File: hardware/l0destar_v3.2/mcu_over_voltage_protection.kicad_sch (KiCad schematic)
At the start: 15 parts

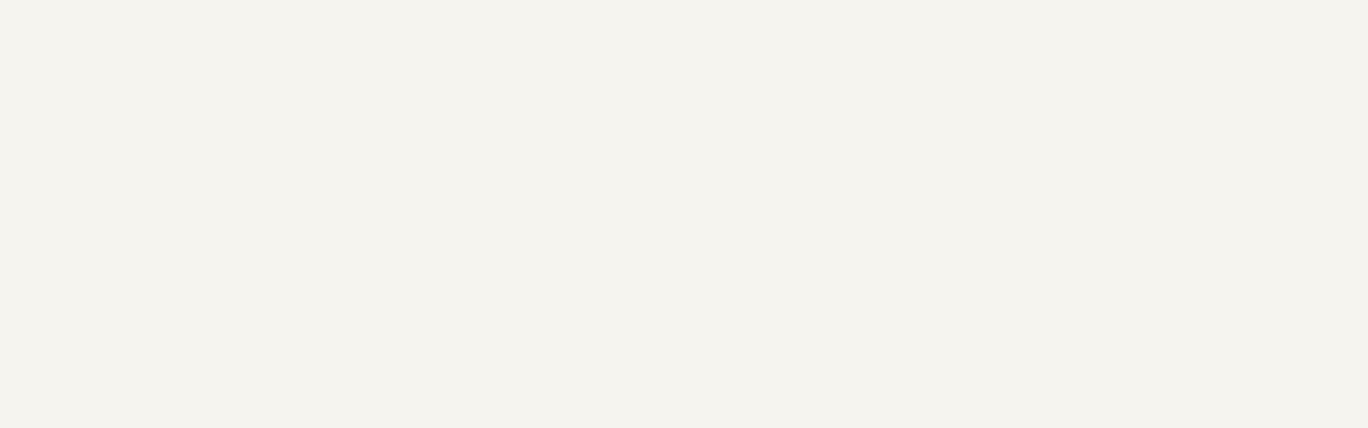
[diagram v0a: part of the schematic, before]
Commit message: update sheet annotations
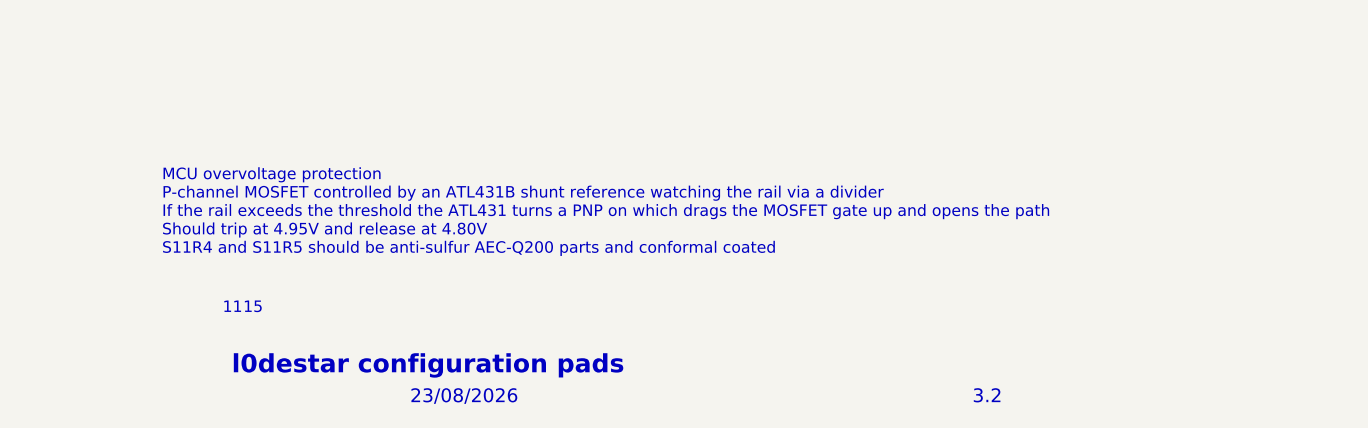
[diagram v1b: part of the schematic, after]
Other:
- note added: "11"
- note added: "15"
- note added: "23/08/2026"
- note added: "3.2"
- note added: "MCU overvoltage protection P-channel MOSFET controlled by an ATL431B shunt reference watching the rail via a divider If the rail exceeds the threshold the ATL431 turns a PNP on which drags the MOSFET gate up and opens the path Should trip at 4.95V and release at 4.80V S11R4 and S11R5 should be anti-sulfur AEC-Q200 parts and conformal coated"
- note added: "l0destar configuration pads"
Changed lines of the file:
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@@
 	(generator_version "10.0")
 	(paper "A4")
+	(text "l0destar configuration pads"
+		(exclude_from_sim no)
+		(at 186.817 189.738 0)
+		(effects
+			(font
+				(face "KiCad Font")
+				(size 2.032 2.032)
+				(thickness 0.4064)
+				(bold yes)
+			)
+			(justify left)
+		)
+	)
+	(text "15"
+		(exclude_from_sim no)
+		(at 188.087 183.388 0)
+		(effects
+			(font
+				(size 1.27 1.27)
+			)
+			(justify left)
+		)
+	)
+	(text "11"
+		(exclude_from_sim no)
+		(at 185.801 183.388 0)
+		(effects
+			(font
+				(size 1.27 1.27)
+			)
+			(justify left)
+		)
+	)
+	(text "3.2"
+		(exclude_from_sim no)
+		(at 269.113 193.294 0)
+		(effects
+			(font
+				(face "KiCad Font")
+				(size 1.524 1.524)
+				(thickness 0.1905)
+			)
+			(justify left)
+		)
+	)
+	(text "MCU overvoltage protection\nP-channel MOSFET controlled by an ATL431B shunt reference watching the rail via a divider\nIf the rail exceeds the threshold the ATL431 turns a PNP on which drags the MOSFET gate up and opens the path\nShould trip at 4.95V and release at 4.80V\nS11R4 and S11R5 should be anti-sulfur AEC-Q200 parts and conformal coated"
+		(exclude_from_sim no)
+		(at 179.07 172.72 0)
+		(effects
+			(font
+				(size 1.27 1.27)
+			)
+			(justify left)
+		)
+	)
+	(text "23/08/2026"
+		(exclude_from_sim no)
+		(at 206.629 193.294 0)
+		(effects
+			(font
+				(face "KiCad Font")
+				(size 1.524 1.524)
+				(thickness 0.1905)
+			)
+			(justify left)
+		)
+	)
 	(junction
 		(at 220.345 46.355)

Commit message: update sheet annotations
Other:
- note added: "MCU overvoltage protection P-channel MOSFET controlled by an ATL431B shunt reference watching the rail via a divider If the rail exceeds the threshold the ATL431 turns a PNP on which drags the MOSFET gate up and opens the path Should trip at 4.95V and release at 4.80V S11R4 and S11R5 should be anti-sulfur AEC-Q200 parts and conformal coated Ideal diode for reverse current protection and bulk cera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"
- note removed: "MCU overvoltage protection P-channel MOSFET controlled by an ATL431B shunt reference watching the rail via a divider If the rail exceeds the threshold the ATL431 turns a PNP on which drags the MOSFET gate up and opens the path Should trip at 4.95V and release at 4.80V S11R4 and S11R5 should be anti-sulfur AEC-Q200 parts and conformal coated"
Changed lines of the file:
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@@
 		)
 	)
-	(text "MCU overvoltage protection\nP-channel MOSFET controlled by an ATL431B shunt reference watching the rail via a divider\nIf the rail exceeds the threshold the ATL431 turns a PNP on which drags the MOSFET gate up and opens the path\nShould trip at 4.95V and release at 4.80V\nS11R4 and S11R5 should be anti-sulfur AEC-Q200 parts and conformal coated"
+	(text "MCU overvoltage protection\nP-channel MOSFET controlled by an ATL431B shunt reference watching the rail via a divider\nIf the rail exceeds the threshold the ATL431 turns a PNP on which drags the MOSFET gate up and opens the path\nShould trip at 4.95V and release at 4.80V\nS11R4 and S11R5 should be anti-sulfur AEC-Q200 parts and conformal coated\nIdeal diode for reverse current protection and bulk ceramics"
 		(exclude_from_sim no)
-		(at 179.07 172.72 0)
+		(at 179.07 173.355 0)
 		(effects
 			(font

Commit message: fix sheet annotations
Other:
- note added: "l0destar MCU over-voltage protection"
- note removed: "l0destar configuration pads"
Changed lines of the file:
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@@
 	(generator_version "10.0")
 	(paper "A4")
-	(text "l0destar configuration pads"
+	(text "l0destar MCU over-voltage protection"
 		(exclude_from_sim no)
 		(at 186.817 189.738 0)
